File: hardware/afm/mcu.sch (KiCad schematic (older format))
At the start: 22 parts

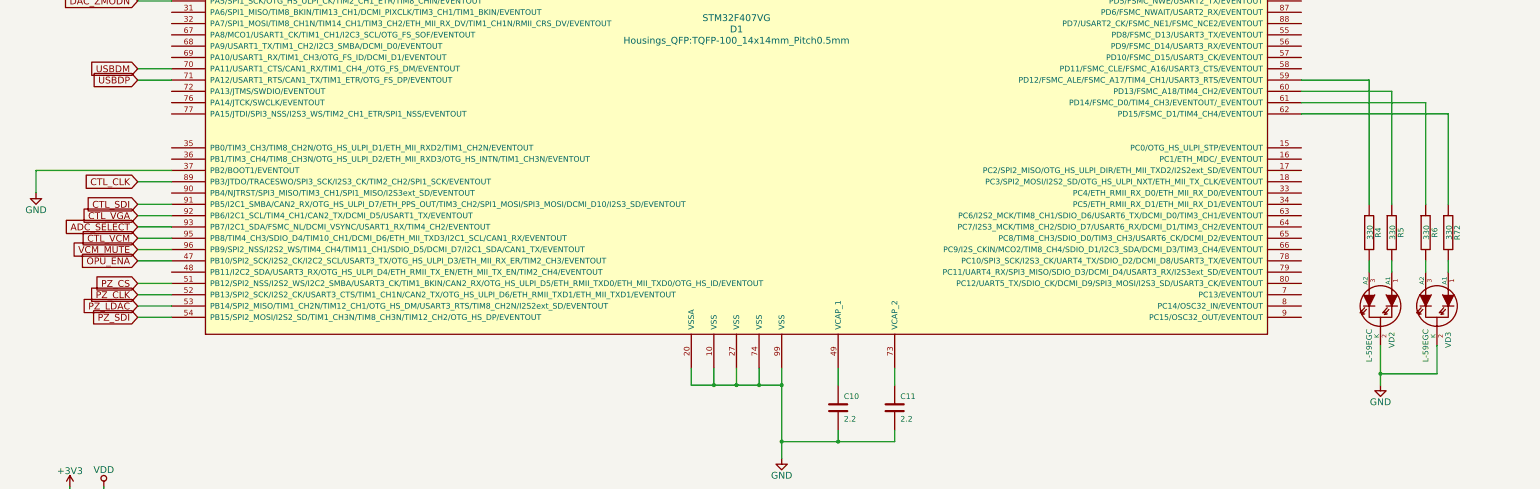
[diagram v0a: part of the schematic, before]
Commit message: Piezo DAC moved from SPI2 to SPI3
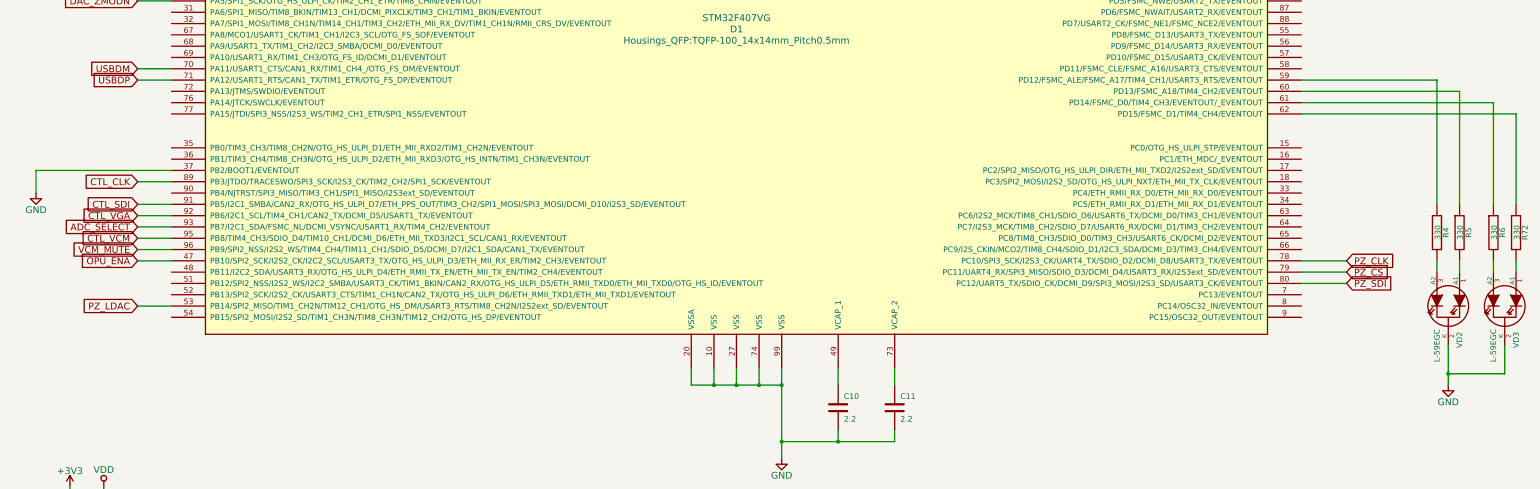
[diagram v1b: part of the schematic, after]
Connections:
- net PZ_CLK: now also D1.78 (PC10/SPI3_SCK/I2S3_CK/UART4_TX/SDIO_D2/DCMI_D8/USART3_TX/EVENTOUT); no longer D1.52 (PB13/SPI2_SCK/I2S2_CK/USART3_CTS/TIM1_CH1N/CAN2_TX/OTG_HS_ULPI_D6/ETH_RMII_TXD1/ETH_MII_TXD1/EVENTOUT)
- net PZ_CS: now also D1.79 (PC11/UART4_RX/SPI3_MISO/SDIO_D3/DCMI_D4/USART3_RX/I2S3ext_SD/EVENTOUT); no longer D1.51 (PB12/SPI2_NSS/I2S2_WS/I2C2_SMBA/USART3_CK/TIM1_BKIN/CAN2_RX/OTG_HS_ULPI_D5/ETH_RMII_TXD0/ETH_MII_TXD0/OTG_HS_ID/EVENTOUT)
- net PZ_SDI: now also D1.80 (PC12/UART5_TX/SDIO_CK/DCMI_D9/SPI3_MOSI/I2S3_SD/USART3_CK/EVENTOUT); no longer D1.54 (PB15/SPI2_MOSI/I2S2_SD/TIM1_CH3N/TIM8_CH3N/TIM12_CH2/OTG_HS_DP/EVENTOUT)
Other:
- moved on the sheet: R4, R5, R6, R72, VD2, VD3
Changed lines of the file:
@@
 Connection ~ 9300 8900
 Wire Wire Line
-	3400 7500 3100 7500
-Wire Wire Line
-	3400 7600 3100 7600
-Wire Wire Line
-	3400 7800 3100 7800
-Wire Wire Line
 	3400 7700 3100 7700
-Text GLabel 3100 7600 0    60   Input ~ 0
-PZ_CLK
-Text GLabel 3100 7500 0    60   Input ~ 0
-PZ_CS
-Text GLabel 3100 7800 0    60   Input ~ 0
-PZ_SDI
 Text GLabel 3100 7700 0    60   Input ~ 0
 PZ_LDAC
@@
 L BI_LED VD2
 U 1 1 559D86A3
-P 14100 7700
-F 0 "VD2" H 14400 7800 50  0000 C CNN
-F 1 "L-59EGC" H 14450 7600 50  0000 C CNN
-F 2 "LEDs:LED-5MM-3" H 14100 7700 60  0001 C CNN
-F 3 "" H 14100 7700 60  0000 C CNN
-	1    14100 7700
+P 14700 7700
+F 0 "VD2" H 15000 7800 50  0000 C CNN
+F 1 "L-59EGC" H 15050 7600 50  0000 C CNN
+F 2 "LEDs:LED-5MM-3" H 14700 7700 60  0001 C CNN
+F 3 "" H 14700 7700 60  0000 C CNN
+	1    14700 7700
 	0    1    1    0
 $EndComp
@@
 L BI_LED VD3
 U 1 1 559D8744
-P 14600 7700
-F 0 "VD3" H 14900 7800 50  0000 C CNN
-F 1 "L-59EGC" H 14950 7600 50  0000 C CNN
-F 2 "LEDs:LED-5MM-3" H 14600 7700 60  0001 C CNN
-F 3 "" H 14600 7700 60  0000 C CNN
-	1    14600 7700
+P 15200 7700
+F 0 "VD3" H 15500 7800 50  0000 C CNN
+F 1 "L-59EGC" H 15550 7600 50  0000 C CNN
+F 2 "LEDs:LED-5MM-3" H 15200 7700 60  0001 C CNN
+F 3 "" H 15200 7700 60  0000 C CNN
+	1    15200 7700
 	0    1    1    0
 $EndComp
@@
 L R R4
 U 1 1 559D8783
-P 14000 7050
-F 0 "R4" V 14080 7050 50  0000 C CNN
-F 1 "330" V 14007 7051 50  0000 C CNN
-F 2 "Resistors_SMD:R_0603_HandSoldering" V 13930 7050 30  0001 C CNN
-F 3 "" H 14000 7050 30  0000 C CNN
-	1    14000 7050
+P 14600 7050
+F 0 "R4" V 14680 7050 50  0000 C CNN
+F 1 "330" V 14607 7051 50  0000 C CNN
+F 2 "Resistors_SMD:R_0603_HandSoldering" V 14530 7050 30  0001 C CNN
+F 3 "" H 14600 7050 30  0000 C CNN
+	1    14600 7050
 	1    0    0    -1
 $EndComp
@@
 L R R5
 U 1 1 559D8804
-P 14200 7050
-F 0 "R5" V 14280 7050 50  0000 C CNN
-F 1 "330" V 14207 7051 50  0000 C CNN
-F 2 "Resistors_SMD:R_0603_HandSoldering" V 14130 7050 30  0001 C CNN
-F 3 "" H 14200 7050 30  0000 C CNN
-	1    14200 7050
+P 14800 7050
+F 0 "R5" V 14880 7050 50  0000 C CNN
+F 1 "330" V 14807 7051 50  0000 C CNN
+F 2 "Resistors_SMD:R_0603_HandSoldering" V 14730 7050 30  0001 C CNN
+F 3 "" H 14800 7050 30  0000 C CNN
+	1    14800 7050
 	1    0    0    -1
 $EndComp
@@
 L R R6
 U 1 1 559D8821
-P 14500 7050
-F 0 "R6" V 14580 7050 50  0000 C CNN
-F 1 "330" V 14507 7051 50  0000 C CNN
-F 2 "Resistors_SMD:R_0603_HandSoldering" V 14430 7050 30  0001 C CNN
-F 3 "" H 14500 7050 30  0000 C CNN
-	1    14500 7050
+P 15100 7050
+F 0 "R6" V 15180 7050 50  0000 C CNN
+F 1 "330" V 15107 7051 50  0000 C CNN
+F 2 "Resistors_SMD:R_0603_HandSoldering" V 15030 7050 30  0001 C CNN
+F 3 "" H 15100 7050 30  0000 C CNN
+	1    15100 7050
 	1    0    0    -1
 $EndComp
@@
 L R R72
 U 1 1 559D883C
-P 14700 7050
-F 0 "R72" V 14780 7050 50  0000 C CNN
-F 1 "330" V 14707 7051 50  0000 C CNN
-F 2 "Resistors_SMD:R_0603_HandSoldering" V 14630 7050 30  0001 C CNN
-F 3 "" H 14700 7050 30  0000 C CNN
-	1    14700 7050
-	1    0    0    -1
-$EndComp
-Wire Wire Line
-	14000 5700 14000 6800
-Wire Wire Line
-	14200 5800 14200 6800
-Wire Wire Line
-	14500 5900 14500 6800
-Wire Wire Line
-	14700 6000 14700 6800
+P 15300 7050
+F 0 "R72" V 15380 7050 50  0000 C CNN
+F 1 "330" V 15307 7051 50  0000 C CNN
+F 2 "Resistors_SMD:R_0603_HandSoldering" V 15230 7050 30  0001 C CNN
+F 3 "" H 15300 7050 30  0000 C CNN
+	1    15300 7050
+	1    0    0    -1
+$EndComp
+Wire Wire Line
+	14600 5700 14600 6800
+Wire Wire Line
+	14800 5800 14800 6800
+Wire Wire Line
+	15100 5900 15100 6800
+Wire Wire Line
+	15300 6000 15300 6800
 $Comp
 L GND #PWR12
 U 1 1 559D8A4D
-P 14100 8400
-F 0 "#PWR12" H 14100 8150 60  0001 C CNN
-F 1 "GND" H 14100 8250 60  0000 C CNN
-F 2 "" H 14100 8400 60  0000 C CNN
-F 3 "" H 14100 8400 60  0000 C CNN
-	1    14100 8400
-	1    0    0    -1
-$EndComp
-Wire Wire Line
-	14100 8400 14100 8050
-Wire Wire Line
-	14100 8300 14600 8300
-Wire Wire Line
-	14600 8300 14600 8050
-Connection ~ 14100 8300
-Wire Wire Line
-	14000 7400 14000 7300
-Wire Wire Line
-	14200 7400 14200 7300
-Wire Wire Line
-	14500 7400 14500 7300
-Wire Wire Line
-	14700 7400 14700 7300
-Wire Wire Line
-	14000 5700 13400 5700
-Wire Wire Line
-	14200 5800 13400 5800
-Wire Wire Line
-	14500 5900 13400 5900
-Wire Wire Line
-	14700 6000 13400 6000
+P 14700 8400
+F 0 "#PWR12" H 14700 8150 60  0001 C CNN
+F 1 "GND" H 14700 8250 60  0000 C CNN
+F 2 "" H 14700 8400 60  0000 C CNN
+F 3 "" H 14700 8400 60  0000 C CNN
+	1    14700 8400
+	1    0    0    -1
+$EndComp
+Wire Wire Line
+	14700 8400 14700 8050
+Wire Wire Line
+	14700 8300 15200 8300
+Wire Wire Line
+	15200 8300 15200 8050
+Connection ~ 14700 8300
+Wire Wire Line
+	14600 7400 14600 7300
+Wire Wire Line
+	14800 7400 14800 7300
+Wire Wire Line
+	15100 7400 15100 7300
+Wire Wire Line
+	15300 7400 15300 7300
+Wire Wire Line
+	13400 5700 14600 5700
+Wire Wire Line
+	13400 5800 14800 5800
+Wire Wire Line
+	13400 5900 15100 5900
+Wire Wire Line
+	13400 6000 15300 6000
+Wire Wire Line
+	13400 7300 13800 7300
+Text GLabel 13800 7300 2    60   Input ~ 0
+PZ_CLK
+Wire Wire Line
+	13400 7400 13800 7400
+Wire Wire Line
+	13400 7500 13800 7500
+Text GLabel 13800 7400 2    60   Input ~ 0
+PZ_CS
+Text GLabel 13800 7500 2    60   Input ~ 0
+PZ_SDI
 $EndSCHEMATC
